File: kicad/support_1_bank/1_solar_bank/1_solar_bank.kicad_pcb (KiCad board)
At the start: 2 copper layers, 35.6 x 66 mm, 5 parts, among them J1 Screw_Terminal_01x02

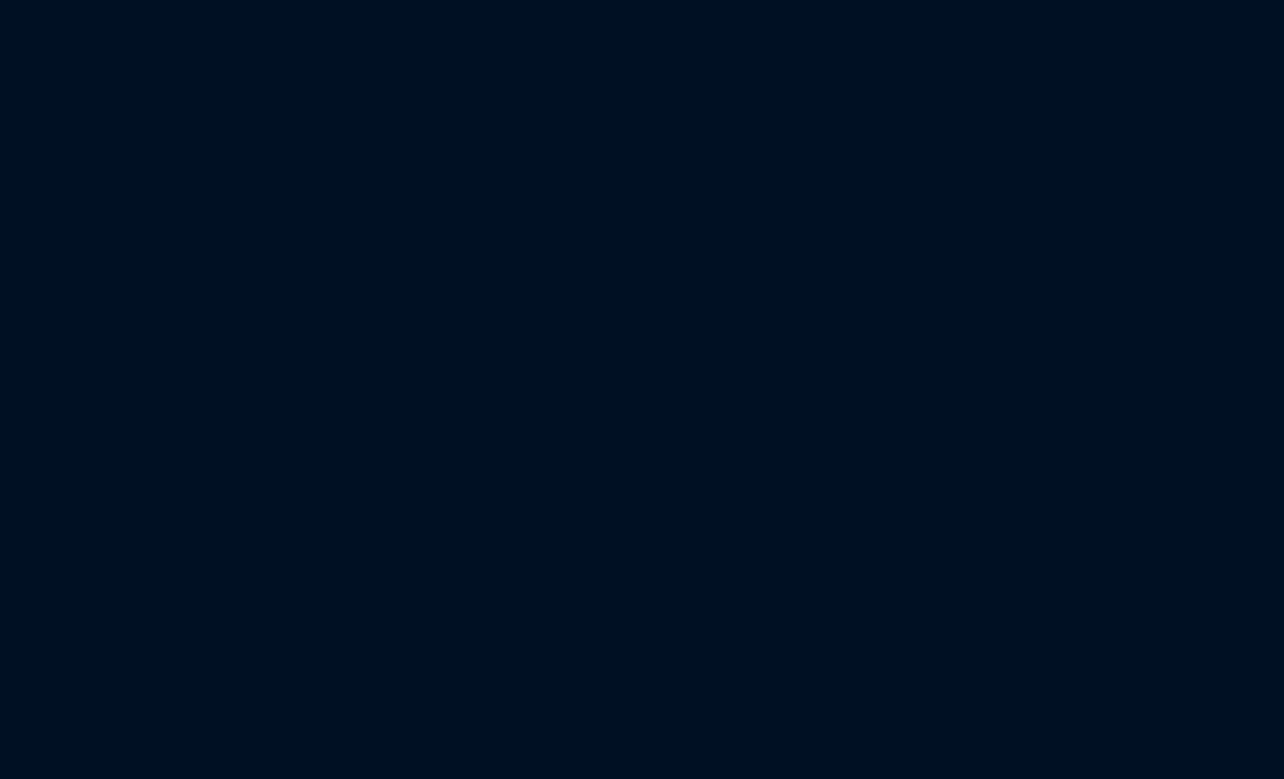
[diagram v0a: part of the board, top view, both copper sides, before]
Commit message: update panel schematic
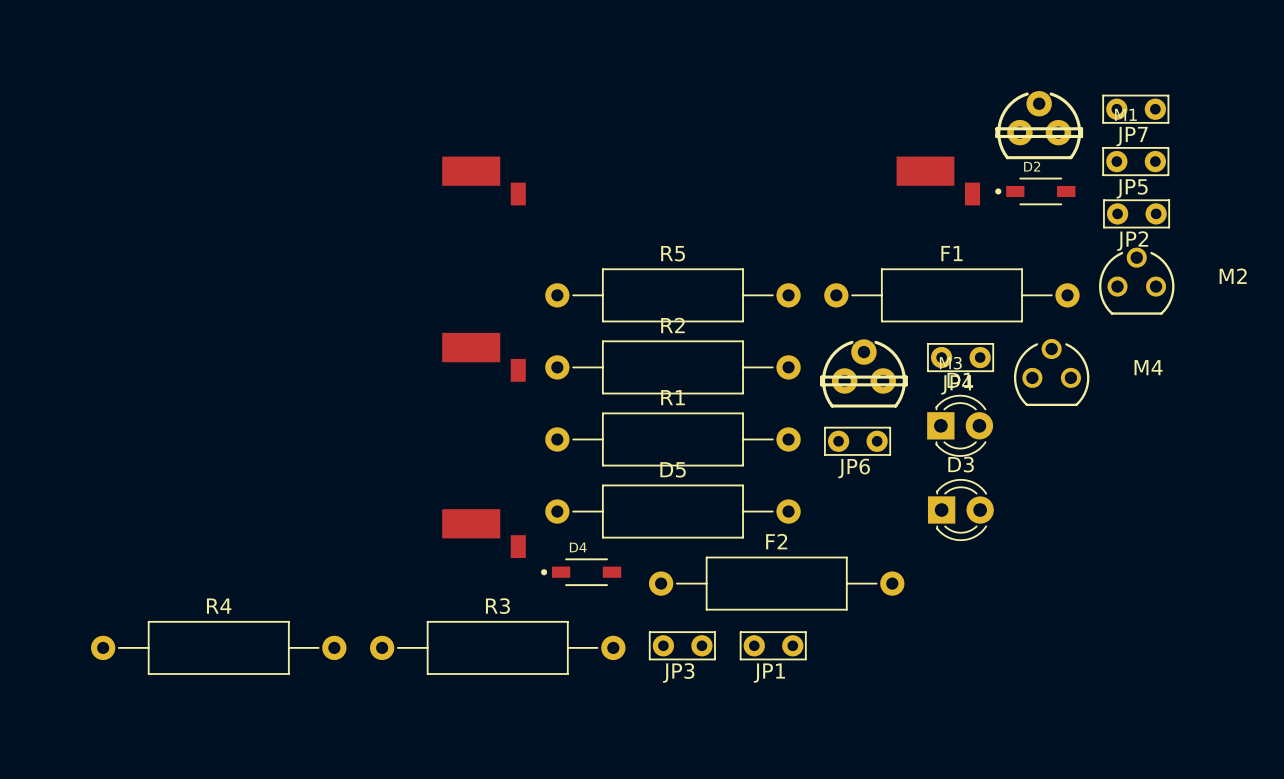
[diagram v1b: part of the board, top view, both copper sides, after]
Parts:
- added D1: LED, panneaux_solaires:LED_D3.0mm, F.Cu at (203.0, 65.9)
- added D2: D_Schottky, panneaux_solaires:SOD3715X135N, F.Cu at (209.6, 50.5)
- added D3: LED, panneaux_solaires:LED_D3.0mm, F.Cu at (203.0, 71.5)
- added D4: D_Schottky, panneaux_solaires:SOD3715X135N, F.Cu at (179.6, 75.6)
- added D5: D_Zener, panneaux_solaires:R_Axial_DIN0309_L9.0mm_D3.2mm_P15.24mm_Horizontal, F.Cu at (177.7, 71.6)
- added F1: Fuse_Small, panneaux_solaires:R_Axial_DIN0309_L9.0mm_D3.2mm_P15.24mm_Horizontal, F.Cu at (196.1, 57.3)
- added F2: Fuse_Small, panneaux_solaires:R_Axial_DIN0309_L9.0mm_D3.2mm_P15.24mm_Horizontal, F.Cu at (184.5, 76.3)
- added JP1: Jumper_2_Bridged, panneaux_solaires:TestPoint_Bridge_Pitch2.54mm_Drill0.7mm, F.Cu at (190.7, 80.4)
- added JP2: Jumper_2_Bridged, panneaux_solaires:TestPoint_Bridge_Pitch2.54mm_Drill0.7mm, F.Cu at (214.6, 51.9)
- added JP3: Jumper_2_Bridged, panneaux_solaires:TestPoint_Bridge_Pitch2.54mm_Drill0.7mm, F.Cu at (184.7, 80.4)
- added JP4: Jumper_2_Bridged, panneaux_solaires:TestPoint_Bridge_Pitch2.54mm_Drill0.7mm, F.Cu at (203.0, 61.4)
- added JP5: Jumper_2_Bridged, panneaux_solaires:TestPoint_Bridge_Pitch2.54mm_Drill0.7mm, F.Cu at (214.6, 48.5)
- added JP6: Jumper_2_Bridged, panneaux_solaires:TestPoint_Bridge_Pitch2.54mm_Drill0.7mm, F.Cu at (196.2, 66.9)
- added JP7: Jumper_2_Bridged, panneaux_solaires:TestPoint_Bridge_Pitch2.54mm_Drill0.7mm, F.Cu at (214.6, 45.0)
- added M1: VN10KM, panneaux_solaires:TO237, F.Cu at (209.5, 46.6)
- added M2: BS250, panneaux_solaires:SOT54E, F.Cu at (215.9, 56.7)
- added M3: VN10KM, panneaux_solaires:TO237, F.Cu at (197.9, 63.0)
- added M4: BS250, panneaux_solaires:SOT54E, F.Cu at (210.3, 62.8)
- added R1: 1M, panneaux_solaires:R_Axial_DIN0309_L9.0mm_D3.2mm_P15.24mm_Horizontal, F.Cu at (177.7, 66.8)
- added R2: 20R, panneaux_solaires:R_Axial_DIN0309_L9.0mm_D3.2mm_P15.24mm_Horizontal, F.Cu at (177.7, 62.1)
- added R3: 1M, panneaux_solaires:R_Axial_DIN0309_L9.0mm_D3.2mm_P15.24mm_Horizontal, F.Cu at (166.2, 80.6)
- added R4: 20R, panneaux_solaires:R_Axial_DIN0309_L9.0mm_D3.2mm_P15.24mm_Horizontal, F.Cu at (147.8, 80.6)
- added R5: 1M, panneaux_solaires:R_Axial_DIN0309_L9.0mm_D3.2mm_P15.24mm_Horizontal, F.Cu at (177.7, 57.3)
- added SC5: Solar_Cell, panneaux_solaires:TRISOLX-T01, F.Cu at (174.0, 77.4)
- added SC6: Solar_Cell, panneaux_solaires:TRISOLX-T01, F.Cu at (204.0, 54.1)
- added SC7: Solar_Cell, panneaux_solaires:TRISOLX-T01, F.Cu at (174.0, 65.7)
- added SC8: Solar_Cell, panneaux_solaires:TRISOLX-T01, F.Cu at (174.0, 54.1)
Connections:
- SC1 pad 1: VCC -> Net-(D2-Pad2)
- SC4 pad 2: GND -> Net-(JP2-Pad1)

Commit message: proto1 panel
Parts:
- J1: value Screw_Terminal_01x02 -> Conn_01x09; footprint TerminalBlock_Phoenix:TerminalBlock_Phoenix_MKDS-1,5-2-5.08_1x02_P5.08mm_Horizontal -> Connector_PinSocket_2.54mm:PinSocket_1x09_P2.54mm_Vertical
- moved JP7 137.2 mm to (90.8, 104.1), turned to 90 degrees
- moved F1 104.9 mm to (119.4, 128.9), turned to 90 degrees
- moved JP4 102.2 mm to (108.6, 100.3), turned to 90 degrees
- moved M4 101.8 mm to (111.8, 88.3), turned to 90 degrees
- moved SC3 100.2 mm to (167.0, 120.0), turned to 0 degrees
- moved M1 99.8 mm to (118.7, 88.3)
- moved D3 99.6 mm to (111.1, 109.9), turned to 90 degrees
- moved M3 97.1 mm to (104.1, 88.3)
- moved R5 95.0 mm to (91.4, 97.2), turned to 90 degrees
- moved M2 94.9 mm to (126.4, 88.3), turned to 90 degrees
- moved D1 94.4 mm to (119.4, 109.9), turned to 90 degrees
- moved F2 90.3 mm to (111.1, 128.9), turned to 90 degrees
- moved JP6 89.7 mm to (113.0, 100.3), turned to 90 degrees
- moved D2 88.6 mm to (134.6, 97.8)
- moved D5 81.8 mm to (96.5, 81.9), turned to 270 degrees
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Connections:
- J1 pad 1: VCC -> +VSW
- JP3 pad 2: VOLTMETER21 -> VOLTMETER1
- JP5 pad 2: AMPERMETER1 -> AMPERMETER2
- M3 pad 2: BNK1_CONTROL -> BNK2_CONTROL
- R4 pad 1: AMPERMETER1 -> AMPERMETER2
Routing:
- net +VSW: track 0.00 -> 185.4 mm, vias 0 -> 2
- net Net-(JP2-Pad1): track 0.00 -> 111.0 mm
- net AMPERMETER2: track 0.00 -> 82.9 mm
- net VOLTMETER1: track 0.00 -> 82.8 mm, vias 0 -> 2
- net AMPERMETER1: track 0.00 -> 81.3 mm
- net VOLTMETER2: track 0.00 -> 69.7 mm, vias 0 -> 4
- net BNK1_CONTROL: track 0.00 -> 37.8 mm, vias 0 -> 2
- net Net-(SC6-Pad2): track 0.00 -> 34.0 mm
- net Net-(SC5-Pad2): track 0.00 -> 33.1 mm
- net Net-(SC7-Pad2): track 0.00 -> 32.9 mm
- net V_REF: track 0.00 -> 27.5 mm
- net Net-(JP4-Pad2): track 0.00 -> 18.2 mm
- net Net-(M3-Pad3): track 0.00 -> 18.1 mm
- net BNK2_CONTROL: track 0.00 -> 18.1 mm, vias 0 -> 2
- net Net-(M1-Pad3): track 0.00 -> 18.1 mm
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- added copper zone on B.Cu, net GND
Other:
- board size 35.6 x 66 mm -> 88.9 x 94 mm

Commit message: revision schemas + pcb
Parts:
- removed D3: LED, panneaux_solaires:LED_D3.0mm
- removed D4: D_Schottky, panneaux_solaires:SOD3715X135N
- removed JP5, JP6: Jumper_2_Bridged, panneaux_solaires:TestPoint_Bridge_Pitch2.54mm_Drill0.7mm
- removed M1, M3: VN10KM, panneaux_solaires:TO237
- removed M2, M4: BS250, panneaux_solaires:SOT54E
- added Q1: RUR040N02HZGTL, panneaux_solaires:RUR040N02HZGTL, F.Cu at (74.9, 48.9)
- added Q2: RUR040N02HZGTL, panneaux_solaires:RUR040N02HZGTL, F.Cu at (69.8, 48.9)
- added Q3: RUR040N02HZGTL, panneaux_solaires:RUR040N02HZGTL, F.Cu at (87.0, 48.9)
- added Q4: RUR040N02HZGTL, panneaux_solaires:RUR040N02HZGTL, F.Cu at (81.9, 48.9)
- added R6: 1M, panneaux_solaires:R_Axial_DIN0309_L9.0mm_D3.2mm_P15.24mm_Horizontal, F.Cu at (82.5, 27.3)
- added R7: 20R, panneaux_solaires:R_Axial_DIN0309_L9.0mm_D3.2mm_P15.24mm_Horizontal, F.Cu at (85.1, 83.8)
- added TP1: TestPoint, panneaux_solaires:TestPoint_Pad_3.0x3.0mm, F.Cu at (104.1, 102.6)
- added TP10: TestPoint, panneaux_solaires:TestPoint_Pad_3.0x3.0mm, F.Cu at (104.4, 25.7)
- added TP11: TestPoint, panneaux_solaires:TestPoint_Pad_3.0x3.0mm, F.Cu at (139.7, 88.1)
- added TP12: TestPoint, panneaux_solaires:TestPoint_Pad_3.0x3.0mm, F.Cu at (104.1, 77.2)
- added TP13: TestPoint, panneaux_solaires:TestPoint_Pad_3.0x3.0mm, F.Cu at (139.4, 77.2)
- added TP14: TestPoint, panneaux_solaires:TestPoint_Pad_3.0x3.0mm, F.Cu at (139.4, 58.2)
- added TP15: TestPoint, panneaux_solaires:TestPoint_Pad_3.0x3.0mm, F.Cu at (104.1, 50.0)
- added TP16: TestPoint, panneaux_solaires:TestPoint_Pad_3.0x3.0mm, F.Cu at (139.2, 39.1)
- added TP2: TestPoint, panneaux_solaires:TestPoint_Pad_3.0x3.0mm, F.Cu at (139.7, 102.6)
- added TP3: TestPoint, panneaux_solaires:TestPoint_Pad_3.0x3.0mm, F.Cu at (104.1, 88.1)
- added TP4: TestPoint, panneaux_solaires:TestPoint_Pad_3.0x3.0mm, F.Cu at (139.4, 69.8)
- added TP5: TestPoint, panneaux_solaires:TestPoint_Pad_3.0x3.0mm, F.Cu at (104.1, 71.1)
- added TP6: TestPoint, panneaux_solaires:TestPoint_Pad_3.0x3.0mm, F.Cu at (104.1, 58.4)
- added TP7: TestPoint, panneaux_solaires:TestPoint_Pad_3.0x3.0mm, F.Cu at (139.4, 50.0)
- added TP8: TestPoint, panneaux_solaires:TestPoint_Pad_3.0x3.0mm, F.Cu at (104.1, 39.1)
- added TP9: TestPoint, panneaux_solaires:TestPoint_Pad_3.0x3.0mm, F.Cu at (139.2, 25.9)
- D1: value LED -> D_Schottky; footprint panneaux_solaires:LED_D3.0mm -> panneaux_solaires:SOD3715X135N
- R1: value 1M -> 20R
- moved JP2 92.4 mm to (74.9, 58.4), turned to 90 degrees
- moved SC3 72.9 mm to (109.2, 75.6), turned to 180 degrees
- moved F2 71.0 mm to (69.8, 71.1), turned to 0 degrees
- moved F1 70.9 mm to (69.8, 78.1), turned to 0 degrees
- moved R3 67.8 mm to (70.5, 27.3), turned to 270 degrees
- moved JP3 66.8 mm to (69.8, 58.4)
- moved R1 63.0 mm to (74.9, 42.5)
- moved J1 58.7 mm to (81.3, 114.3), turned to 90 degrees
- moved R2 52.5 mm to (85.1, 88.9)
- moved JP1 51.8 mm to (87.0, 58.4)
- moved JP4 49.7 mm to (81.9, 58.4)
- moved SC4 47.2 mm to (135.9, 74.3), turned to 0 degrees
- moved D1 46.6 mm to (104.1, 65.8)
- moved SC6 41.0 mm to (135.9, 55.2)
- moved SC5 41.0 mm to (109.2, 56.5)
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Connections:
- D1 pad 2: Net-(D1-Pad2) -> VOLTMETER2
- D2 pad 1: VOLTMETER1 -> Net-(D2-Pad1)
- D2 pad 2: Net-(D2-Pad2) -> VOLTMETER1
- F1 pad 2: Net-(D1-Pad1) -> Net-(D2-Pad1)
- F2 pad 2: Net-(D3-Pad1) -> Net-(D1-Pad1)
- JP1 pad 1: Net-(D1-Pad2) -> Net-(JP1-Pad1)
- JP2 pad 2: AMPERMETER1 -> Net-(JP2-Pad2)
- JP3 pad 1: Net-(D1-Pad2) -> Net-(JP2-Pad1)
- JP3 pad 2: VOLTMETER1 -> AMPERMETER1
- JP4 pad 1: Net-(D3-Pad2) -> Net-(JP1-Pad1)
- JP4 pad 2: Net-(JP4-Pad2) -> AMPERMETER2
- R1 pad 1: Net-(M1-Pad3) -> BNK1_CONTROL
- R3 pad 1: Net-(M3-Pad3) -> +VSW
- R3 pad 2: GND -> Net-(Q1-Pad2)
- R4 pad 1: AMPERMETER2 -> BNK2_CONTROL
- SC1 pad 1: Net-(D2-Pad2) -> VOLTMETER1
- SC5 pad 1: Net-(D4-Pad2) -> VOLTMETER2
- SC8 pad 2: Net-(JP5-Pad1) -> Net-(JP1-Pad1)
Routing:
- net BNK2_CONTROL: track 18.1 -> 94.6 mm
- net Net-(JP1-Pad1): track 0.00 -> 74.6 mm
- net BNK1_CONTROL: track 37.8 -> 102.8 mm, vias 2 -> 1
- net +VSW: track 185.4 -> 122.4 mm, vias 2 -> 0
- net Net-(JP2-Pad1): track 111.0 -> 75.8 mm, vias 0 -> 2
- net VOLTMETER1: track 82.8 -> 48.5 mm, vias 2 -> 0
- net Net-(D2-Pad1): track 0.00 -> 28.6 mm
- net VOLTMETER2: track 69.7 -> 92.9 mm, vias 4 -> 1
- net Net-(JP4-Pad2): track 18.2 -> 0.00 mm
- net Net-(M3-Pad3): track 18.1 -> 0.00 mm
- net Net-(M1-Pad3): track 18.1 -> 0.00 mm
- net Net-(D1-Pad1): track 3.81 -> 20.5 mm
- net Net-(SC2-Pad2): track 28.1 -> 43.6 mm
- net Net-(D3-Pad2): track 12.2 -> 0.00 mm
- net Net-(D1-Pad2): track 12.2 -> 0.00 mm
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- added copper zone on F.Cu, net GND
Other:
- board size 88.9 x 94 mm -> 100 x 100 mm
- board text added: "J3 J2"
- board text added: "J4 J1"
- board text added: "VCC GND VREF VOLT1 AMP1 B1 VOLT2 AMP2 B2"

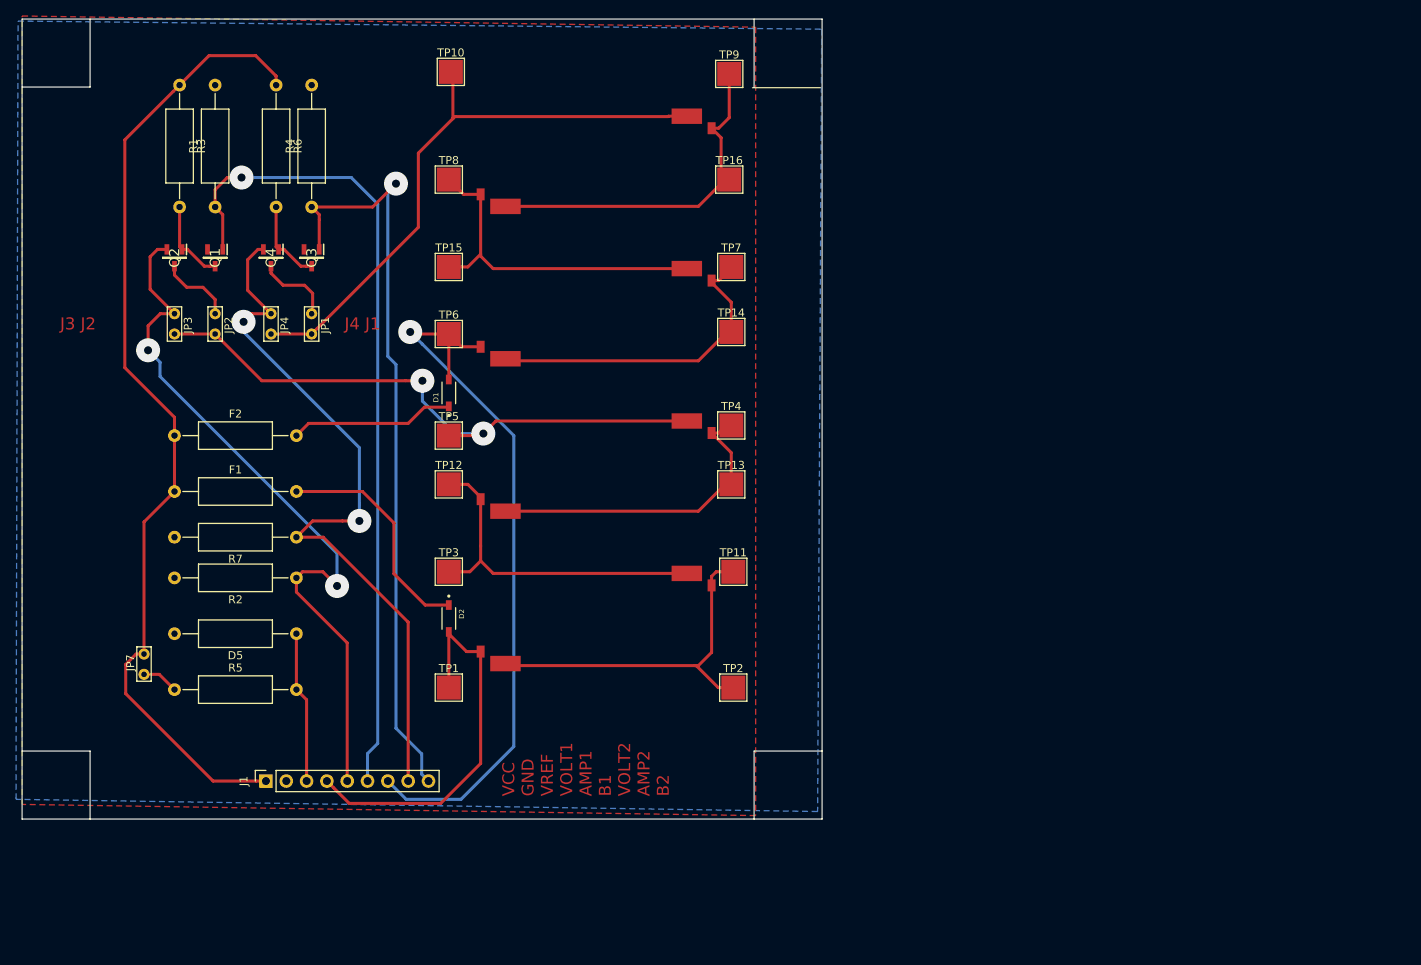
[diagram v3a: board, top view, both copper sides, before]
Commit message: update avec le code du capteur d'horizon
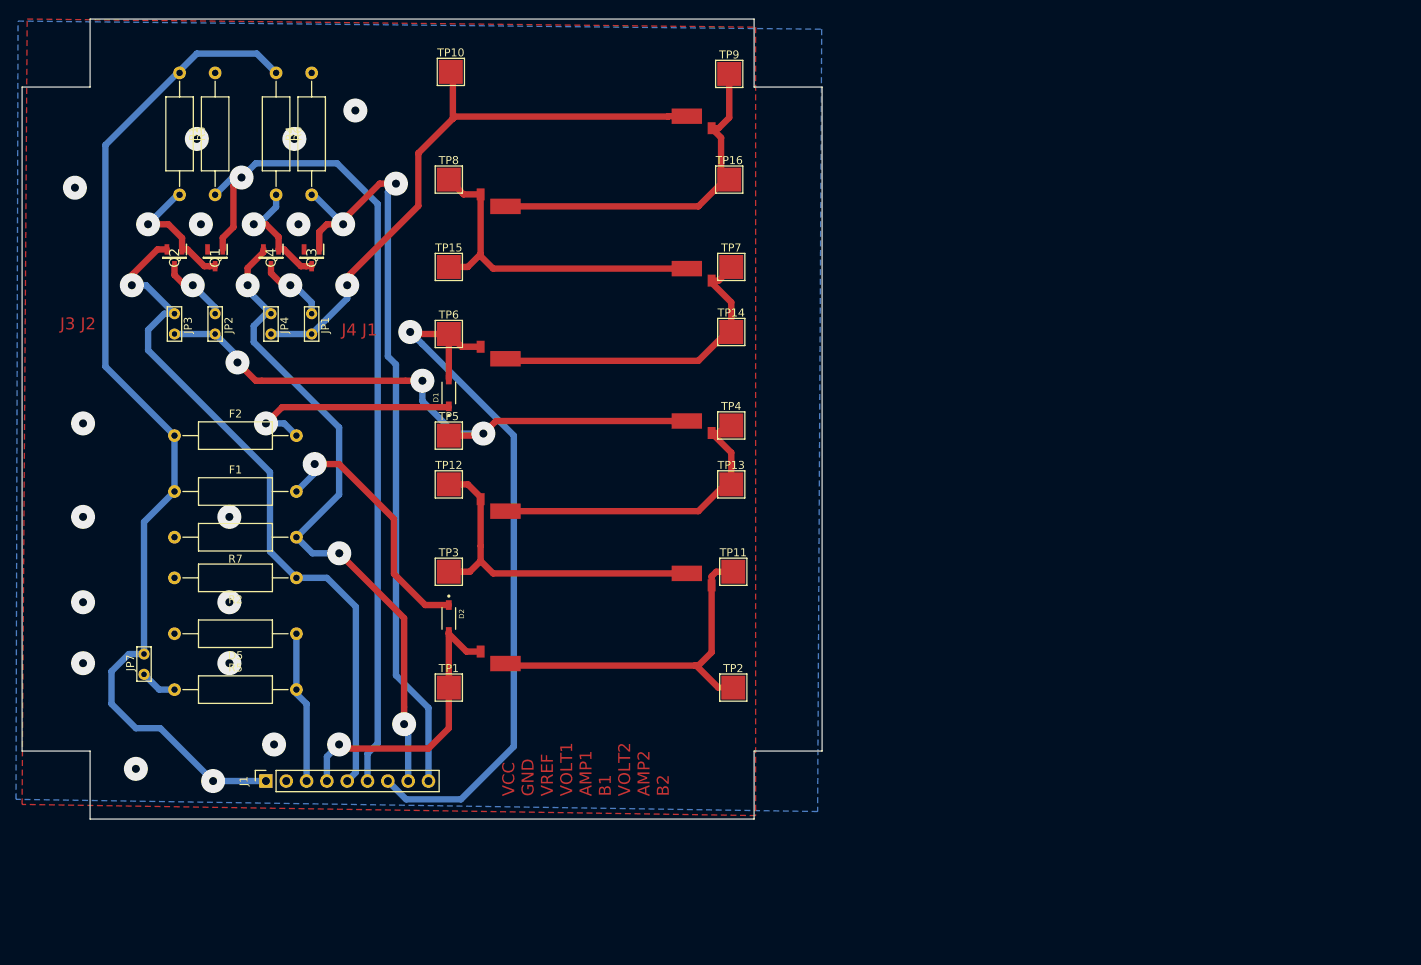
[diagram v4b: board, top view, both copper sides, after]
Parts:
- moved R1 1.52 mm to (74.9, 41.0)
- moved R3 1.52 mm to (70.5, 25.8)
- moved R4 1.52 mm to (87.0, 41.0)
- moved R6 1.52 mm to (82.5, 25.8)
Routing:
- net VOLTMETER1: track 48.5 -> 37.4 mm, vias 0 -> 1
- net Net-(D1-Pad1): track 20.5 -> 28.1 mm, vias 0 -> 1
- net AMPERMETER2: track 92.1 -> 84.8 mm, vias 2 -> 3
- net Net-(Q1-Pad2): track 10.4 -> 16.9 mm, vias 0 -> 1
- net +VSW: track 122.4 -> 128.3 mm, vias 0 -> 1
- net Net-(Q3-Pad2): track 10.4 -> 16.0 mm, vias 0 -> 1
- net BNK1_CONTROL: track 102.8 -> 106.7 mm
- net Net-(D2-Pad1): track 28.6 -> 32.5 mm, vias 0 -> 1
- net AMPERMETER1: track 91.2 -> 87.8 mm, vias 2 -> 1
- net BNK2_CONTROL: track 94.6 -> 97.2 mm, vias 2 -> 3
- net Net-(JP1-Pad2): track 9.72 -> 8.87 mm, vias 0 -> 1
- net Net-(JP2-Pad2): track 9.23 -> 8.63 mm, vias 0 -> 1
- net VOLTMETER2: track 92.9 -> 92.4 mm
- net Net-(JP2-Pad1): track 75.8 -> 76.2 mm, vias 2 -> 3
- net Net-(JP1-Pad1): vias 0 -> 1
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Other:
- outline, holes or cut-outs redrawn
- rule trace_min: 0.2 -> 0.8
- rule via_min_size: 0.4 -> 1
